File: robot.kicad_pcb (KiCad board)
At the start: 2 copper layers, 55.2 x 89.3 mm, 77 parts, among them J1 PCA9865 2, J10 BATT out, J11 Vin, J12 I2C, J2 I2S, J3 Programming, J4 IMU, J5 Switches, J6 Expansion, J7 VCC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

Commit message: Board ready to go.
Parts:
- removed J10: BATT out, Connector_PinHeader_2.54mm:Connector_Battery_SolderPads
- removed R10, R11, R12, R13, R14, R15, R16, R17, R18, R19, R20, R21, R22, R23, R24, R9: 220, Resistor_SMD:R_1206_3216Metric_Pad1.30x1.75mm_HandSolder
- removed the REF** at (143.5, 180.3)
- removed the REF** at (99.8, 139.4)
- removed the REF** at (143.5, 111.8)
- removed the REF** at (100.1, 111.8)
- added REF**: MountingHole_2.2mm_M2, MountingHole:MountingHole_2.2mm_M2, F.Cu at (146.9, 126.1)
- added REF**: MountingHole_2.2mm_M2, MountingHole:MountingHole_2.2mm_M2, F.Cu at (98.9, 95.4)
- added REF**: MountingHole_2.2mm_M2, MountingHole:MountingHole_2.2mm_M2, F.Cu at (145.8, 168.0)
- added REF**: MountingHole_2.2mm_M2, MountingHole:MountingHole_2.2mm_M2, F.Cu at (99.6, 181.7)
- added RN1: 220, Resistor_SMD:R_Array_Concave_4x0603, F.Cu at (115.1, 156.5)
- added RN2: 220, Resistor_SMD:R_Array_Concave_4x0603, F.Cu at (125.7, 156.5)
- added RN3: 220, Resistor_SMD:R_Array_Concave_4x0603, F.Cu at (110.2, 143.5)
- added RN4: 220, Resistor_SMD:R_Array_Concave_4x0603, F.Cu at (131.1, 144.5)
- moved J6 89.7 mm to (98.7, 127.7), turned to 180 degrees
- moved C12 47.1 mm to (143.8, 148.2)
- moved SW4 43.9 mm to (101.5, 133.7), turned to 180 degrees
- moved J7 42.4 mm to (139.6, 187.1), turned to -90 degrees
- moved J12 40.6 mm to (150.1, 113.0)
- moved C11 40.1 mm to (149.2, 154.2), turned to -90 degrees
- moved C10 32.6 mm to (139.7, 170.6), turned to 180 degrees
- moved C9 29.7 mm to (149.6, 161.4), turned to 90 degrees
- moved J11 29.0 mm to (120.6, 187.1), turned to -90 degrees
- moved U6 27.4 mm to (144.5, 162.4), turned to 90 degrees
- moved J5 24.0 mm to (145.1, 95.0)
- moved R28 22.5 mm to (105.3, 129.0), turned to 90 degrees
- moved D3 21.9 mm to (102.4, 125.0), turned to -90 degrees
- moved D1 17.2 mm to (113.5, 129.8)
- moved R7 15.1 mm to (111.5, 134.6), turned to 90 degrees
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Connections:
- J5 pad 1: VCC -> GND
- J5 pad 10: GND -> /SWITCH_1
- J5 pad 11: /SWITCH_4 -> GND
- J5 pad 12: GND -> /SWITCH_0
- J5 pad 13: /SWITCH_5 -> GND
- J5 pad 14: unconnected-(J5-Pad14) -> VCC
- J5 pad 2: GND -> /SWITCH_5
- J5 pad 3: /SWITCH_0 -> GND
- J5 pad 4: GND -> /SWITCH_4
- J5 pad 5: /SWITCH_1 -> GND
- J5 pad 6: GND -> /SWITCH_3
- J5 pad 7: /SWITCH_2 -> GND
- J5 pad 8: GND -> /SWITCH_2
- J5 pad 9: /SWITCH_3 -> GND
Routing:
- net GND: track 362.1 -> 463.7 mm, vias 12 -> 13
- net +BATT: track 33.1 -> 75.2 mm, vias 2 -> 0
- net Net-(C8-Pad2): track 16.9 -> 57.5 mm
- net Net-(C10-Pad2): track 0.00 -> 31.3 mm
- net IO_0: track 23.5 -> 49.1 mm
- net /ESP32_TX: track 2.52 -> 27.1 mm, vias 0 -> 1
- net /ESP32_RX: track 5.17 -> 29.1 mm, vias 1 -> 0
- net +5V: track 65.9 -> 89.3 mm
- net /SWITCH_5: track 20.9 -> 44.2 mm, vias 1 -> 2
- net IO_39: track 0.00 -> 23.1 mm, vias 0 -> 2
- net Net-(JP4-Pad7): track 26.3 -> 4.31 mm
- net VCC: track 222.7 -> 244.2 mm, vias 2 -> 5
- net Net-(JP1-Pad1): track 27.7 -> 6.45 mm, vias 1 -> 0
- net /PWM3: track 40.7 -> 19.5 mm
- net IO_36: track 0.00 -> 20.4 mm, vias 0 -> 2
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- removed copper zone on B.Cu, net GND
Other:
- board size 55.2 x 89.3 mm -> 56.3 x 97.2 mm
- board text added: "ROBOT (c)2022 J.Hudson"
- board text removed: "J1"

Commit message: Clean chematic
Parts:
- removed REF** (x4): MountingHole_2.2mm_M2, MountingHole:MountingHole_2.2mm_M2
- added C13: 104, Capacitor_SMD:C_1206_3216Metric_Pad1.33x1.80mm_HandSolder, F.Cu at (116.3, 165.0)
- added C14: 106, Capacitor_SMD:C_1210_3225Metric_Pad1.33x2.70mm_HandSolder, F.Cu at (121.0, 168.5)
- added J10: Servo pwr, Connector_PinHeader_2.54mm:Connector_SolderPadsx3, F.Cu at (98.2, 168.8)
- added J13: VCC, Connector_PinHeader_2.54mm:PinHeader_1x02_P2.54mm_Vertical, F.Cu at (99.8, 94.9)
- added JP6: HEADER-3X04, Adafruit:3X04, F.Cu at (140.7, 182.6)
- added JP7: HEADER-3X04, Adafruit:3X04, F.Cu at (106.8, 173.2)
- added JP8: HEADER-3X04, Adafruit:3X04, F.Cu at (140.8, 173.2)
- added JP9: HEADER-3X04, Adafruit:3X04, F.Cu at (106.6, 182.2)
- added R9: 10K, Resistor_SMD:R_1206_3216Metric_Pad1.30x1.75mm_HandSolder, F.Cu at (115.7, 182.0)
- added RN5: 220, Resistor_SMD:R_Array_Concave_4x0603, F.Cu at (132.3, 178.7)
- added RN6: 220, Resistor_SMD:R_Array_Concave_4x0603, F.Cu at (114.6, 169.3)
- added RN7: 220, Resistor_SMD:R_Array_Concave_4x0603, F.Cu at (133.7, 169.2)
- added RN8: 220, Resistor_SMD:R_Array_Concave_4x0603, F.Cu at (115.7, 177.8)
- added U7: PCA9685PW, Package_SO:TSSOP-28_4.4x9.7mm_P0.65mm, F.Cu at (123.7, 177.8)
- moved C12 50.3 mm to (147.2, 198.4), turned to 180 degrees
- moved U6 43.9 mm to (141.4, 206.2), turned to 0 degrees
- moved C11 35.7 mm to (145.4, 189.6), turned to 180 degrees
- moved C9 33.8 mm to (141.4, 194.2)
- moved J1 32.1 mm to (149.4, 153.8), turned to 0 degrees
- moved U3 22.9 mm to (128.7, 206.2)
- moved C4 20.9 mm to (122.2, 193.6)
- moved C5 20.9 mm to (116.1, 196.2)
- moved C8 20.9 mm to (110.6, 190.6)
- moved F1 20.9 mm to (105.2, 200.4)
- moved J11 20.9 mm to (120.6, 208.0)
- moved J9 20.9 mm to (98.0, 197.2)
- moved R26 20.9 mm to (116.1, 192.9)
- moved SW5 20.9 mm to (104.4, 207.9)
- moved U4 20.9 mm to (118.6, 188.6)
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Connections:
- RN1 pad 1: /PWM0 -> /servos/PWM3
- RN1 pad 2: /PWM1 -> /servos/PWM2
- RN1 pad 3: /PWM2 -> /servos/PWM1
- RN1 pad 4: /PWM3 -> /servos/PWM0
- RN2 pad 1: /PWM8 -> /servos/PWM11
- RN2 pad 2: /PWM9 -> /servos/PWM10
- RN2 pad 3: /PWM10 -> /servos/PWM9
- RN2 pad 4: /PWM11 -> /servos/PWM8
- RN3 pad 5: /PWM4 -> /servos/PWM7
- RN3 pad 6: /PWM5 -> /servos/PWM6
- RN3 pad 7: /PWM6 -> /servos/PWM5
- RN3 pad 8: /PWM7 -> /servos/PWM4
- RN4 pad 5: /PWM12 -> /servos/PWM15
- RN4 pad 6: /PWM13 -> /servos/PWM14
- RN4 pad 7: /PWM14 -> /servos/PWM13
- RN4 pad 8: /PWM15 -> /servos/PWM12
- U2 pad 10: /PWM4 -> /servos/PWM4
- U2 pad 11: /PWM5 -> /servos/PWM5
- U2 pad 12: /PWM6 -> /servos/PWM6
- U2 pad 13: /PWM7 -> /servos/PWM7
- U2 pad 15: /PWM8 -> /servos/PWM8
- U2 pad 16: /PWM9 -> /servos/PWM9
- U2 pad 17: /PWM10 -> /servos/PWM10
- U2 pad 18: /PWM11 -> /servos/PWM11
- U2 pad 19: /PWM12 -> /servos/PWM12
- U2 pad 20: /PWM13 -> /servos/PWM13
- U2 pad 21: /PWM14 -> /servos/PWM14
- U2 pad 22: /PWM15 -> /servos/PWM15
- U2 pad 6: /PWM0 -> /servos/PWM0
- U2 pad 7: /PWM1 -> /servos/PWM1
- U2 pad 8: /PWM2 -> /servos/PWM2
- U2 pad 9: /PWM3 -> /servos/PWM3
- U4 pad 4: +5V -> +5VL
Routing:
- net GND: track 463.7 -> 595.8 mm, vias 13 -> 16
- net +5VL: track 0.00 -> 69.3 mm
- net VCC: track 244.2 -> 308.5 mm, vias 5 -> 6
- net +5VA: track 0.00 -> 48.9 mm
- net +5VD: track 65.9 -> 100.1 mm, vias 1 -> 2
- net WIRE_1_SCL: track 97.7 -> 127.9 mm
- net WIRE_1_SDA: track 85.6 -> 114.8 mm, vias 4 -> 5
- net ONEWIRE_BUS: track 62.2 -> 90.7 mm, vias 3 -> 5
- net /servos/PWM3: track 0.00 -> 24.7 mm, vias 0 -> 2
- net /PWM0: track 24.4 -> 0.00 mm, vias 2 -> 0
- net /PWM1: track 23.2 -> 0.00 mm, vias 2 -> 0
- net /servos/PWM0: track 0.00 -> 22.3 mm, vias 0 -> 2
- net /PWM2: track 21.6 -> 0.00 mm, vias 2 -> 0
- net /servos/PWM1: track 0.00 -> 20.1 mm, vias 0 -> 2
- net /PWM3: track 19.5 -> 0.00 mm, vias 2 -> 0
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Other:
- board size 56.3 x 97.2 mm -> 56.3 x 118.2 mm

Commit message: Cleaned revision 2.
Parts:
- added ?: , , F.Cu at (98.5, 189.6)
- added ?: , , F.Cu at (146.6, 125.6)
- added ?: , , F.Cu at (150.4, 208.4)
- added ?: , , F.Cu at (103.2, 98.3)
- moved R27 9.18 mm to (117.3, 130.7), turned to 90 degrees
- moved C2 1.07 mm to (114.5, 134.7)
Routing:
- net VCC: track 308.5 -> 297.5 mm
- net IO_0: track 60.1 -> 54.6 mm
- net Net-(C10-Pad2): track 20.3 -> 22.7 mm
- net ONEWIRE_BUS: vias 5 -> 4

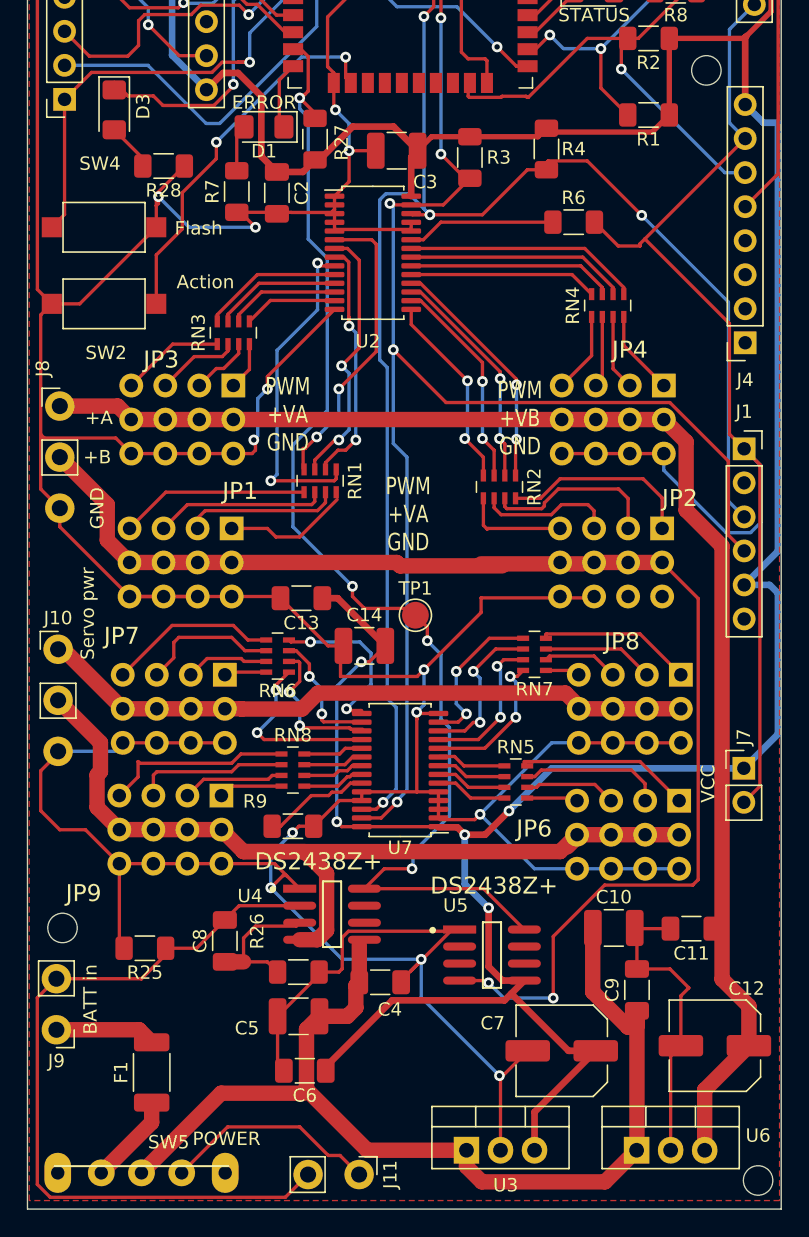
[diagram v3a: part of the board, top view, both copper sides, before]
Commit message: Very minor tweaks for board version 3.
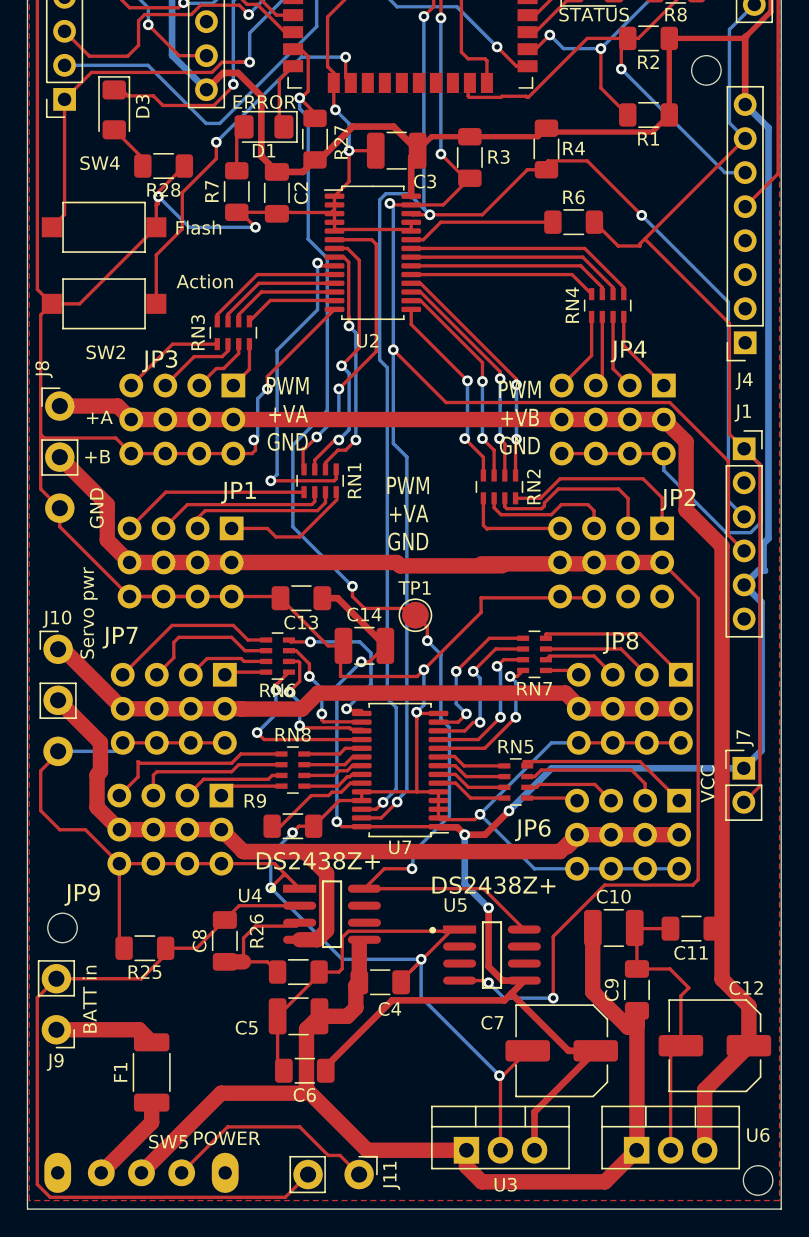
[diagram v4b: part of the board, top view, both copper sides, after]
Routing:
- net VCC: track 297.5 -> 294.6 mm

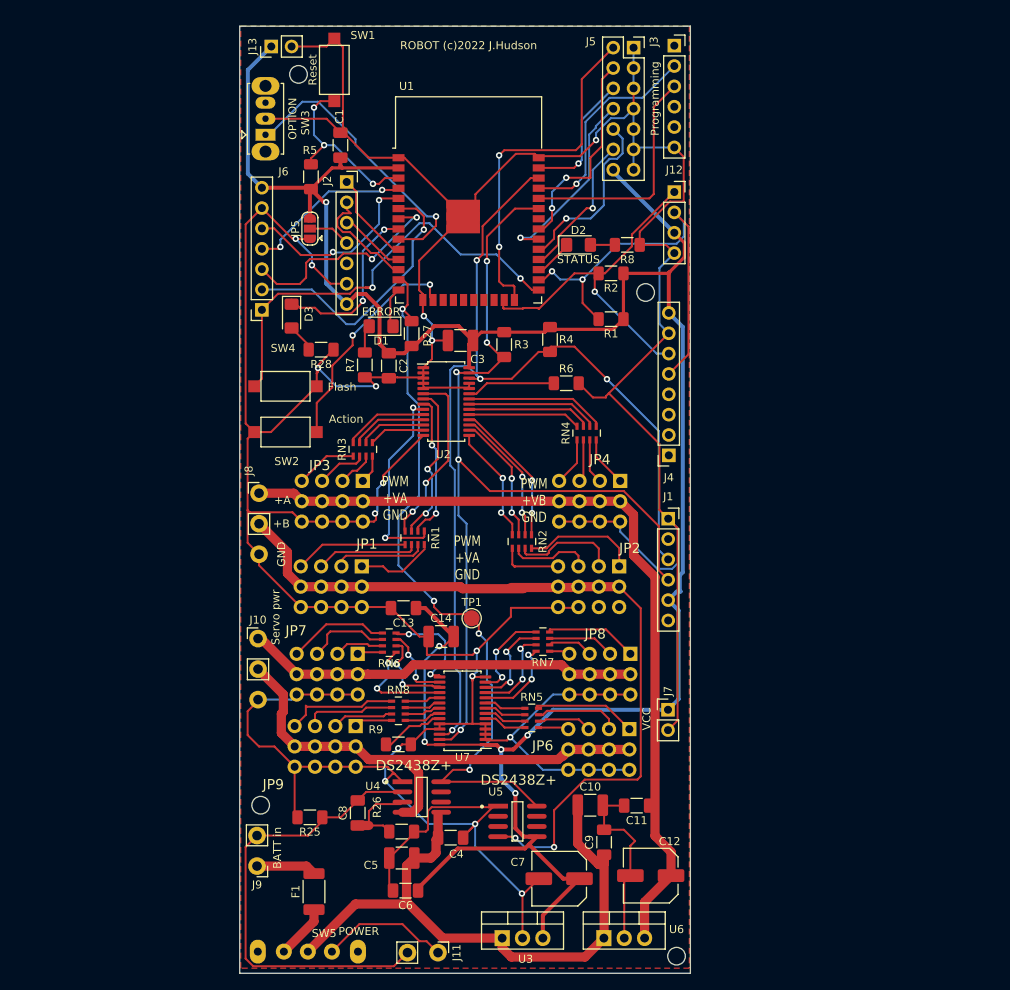
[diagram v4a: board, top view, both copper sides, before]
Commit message: Upgrade to version 7, started adding new WROOM-S3
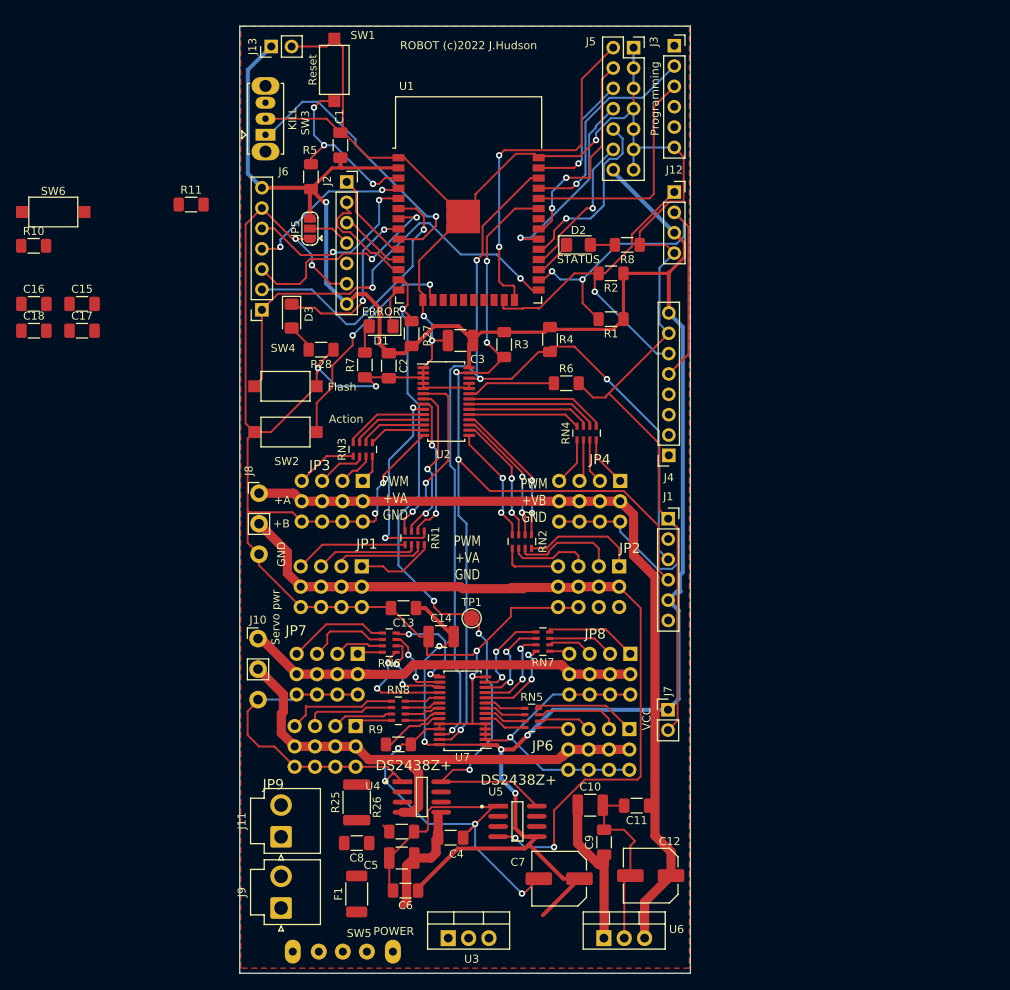
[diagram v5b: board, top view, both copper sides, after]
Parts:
- removed ? (x4): , 
- added C15: 104, Capacitor_SMD:C_1206_3216Metric_Pad1.33x1.80mm_HandSolder, F.Cu at (76.2, 127.0)
- added C16: 104, Capacitor_SMD:C_1206_3216Metric_Pad1.33x1.80mm_HandSolder, F.Cu at (70.2, 127.0)
- added C17: 104, Capacitor_SMD:C_1206_3216Metric_Pad1.33x1.80mm_HandSolder, F.Cu at (76.2, 130.3)
- added C18: 104, Capacitor_SMD:C_1206_3216Metric_Pad1.33x1.80mm_HandSolder, F.Cu at (70.2, 130.3)
- added R10: 10K, Resistor_SMD:R_1206_3216Metric_Pad1.30x1.75mm_HandSolder, F.Cu at (70.2, 119.8)
- added R11: 100K, Resistor_SMD:R_1206_3216Metric_Pad1.30x1.75mm_HandSolder, F.Cu at (89.8, 114.6)
- added SW6: OPTION, Button_Switch_SMD:SW_SPST_CK_RS282G05A3, F.Cu at (72.6, 115.5)
- J11, J9: footprint Connector_PinHeader_2.54mm:Connector_Battery_SolderPads -> Connector_JST:JST_VH_B2P-VH-B_1x02_P3.96mm_Vertical
- R25: footprint Resistor_SMD:R_1206_3216Metric_Pad1.30x1.75mm_HandSolder -> Resistor_SMD:R_1812_4532Metric_Pad1.30x3.40mm_HandSolder
- SW3: value OPTION -> KILL
- moved J11 24.3 mm to (101.0, 193.5), turned to 90 degrees
- moved U3 6.73 mm to (121.9, 206.2)
- moved R25 6.13 mm to (110.5, 189.2), turned to 90 degrees
- moved J9 6.04 mm to (101.0, 202.4), turned to 90 degrees
- moved F1 5.34 mm to (110.5, 200.7)
- moved SW5 4.37 mm to (108.8, 207.9)
- moved C8 3.76 mm to (110.5, 194.3), turned to 180 degrees
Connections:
- C10 pad 2: Net-(C10-Pad2) -> GND
- C11 pad 2: Net-(C10-Pad2) -> GND
- C12 pad 2: Net-(C10-Pad2) -> GND
- C9 pad 2: Net-(C10-Pad2) -> GND
- J6 pad 2: IO_34 -> IO_35
- J6 pad 3: IO_35 -> IO_36
- J6 pad 4: IO_36 -> IO_39
- J6 pad 5: IO_39 -> GND
- J6 pad 6: GND -> VCC
- J6 pad 7: VCC -> (no net)
- U6 pad 2: Net-(C10-Pad2) -> GND
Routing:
- net Net-(C8-Pad2): track 57.5 -> 0.00 mm
- net +BATT: track 79.0 -> 35.3 mm
- net Net-(C10-Pad2): track 22.7 -> 0.00 mm
- net Net-(J11-Pad1): track 16.1 -> 0.00 mm
- net GND: track 595.8 -> 607.2 mm
- net Net-(C8-Pad1): track 10.7 -> 1.44 mm
- net Net-(F1-Pad2): track 7.50 -> 0.00 mm
- net Net-(F1-Pad1): track 6.80 -> 0.00 mm
- net VCC: track 294.6 -> 291.7 mm

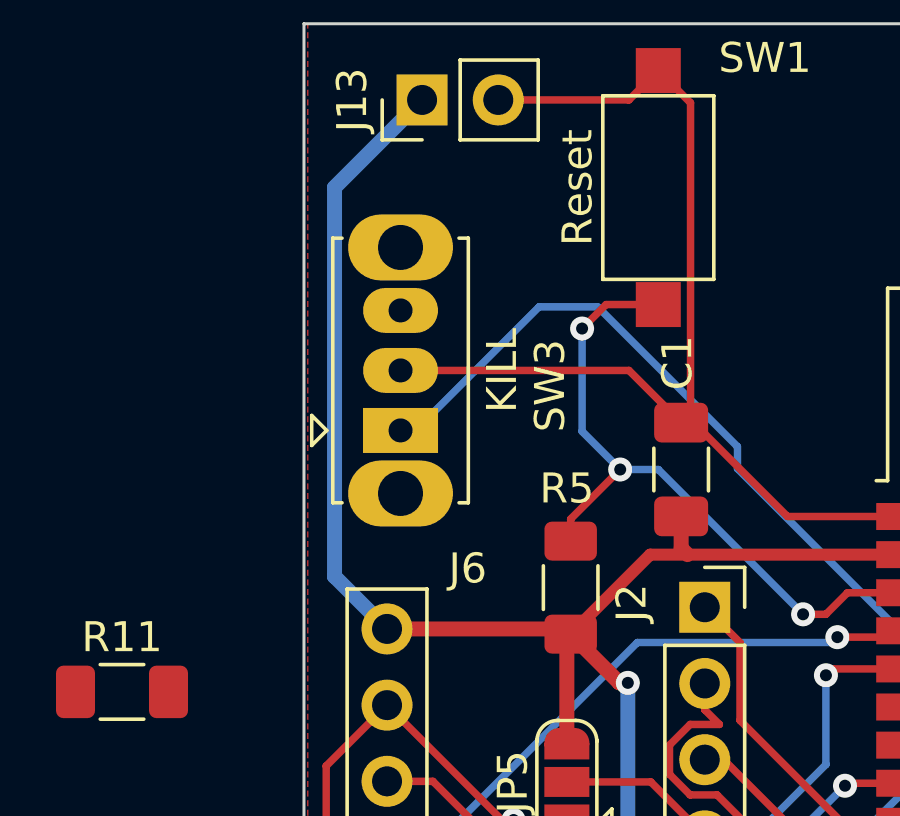
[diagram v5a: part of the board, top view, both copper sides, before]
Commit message: started wiring up s3
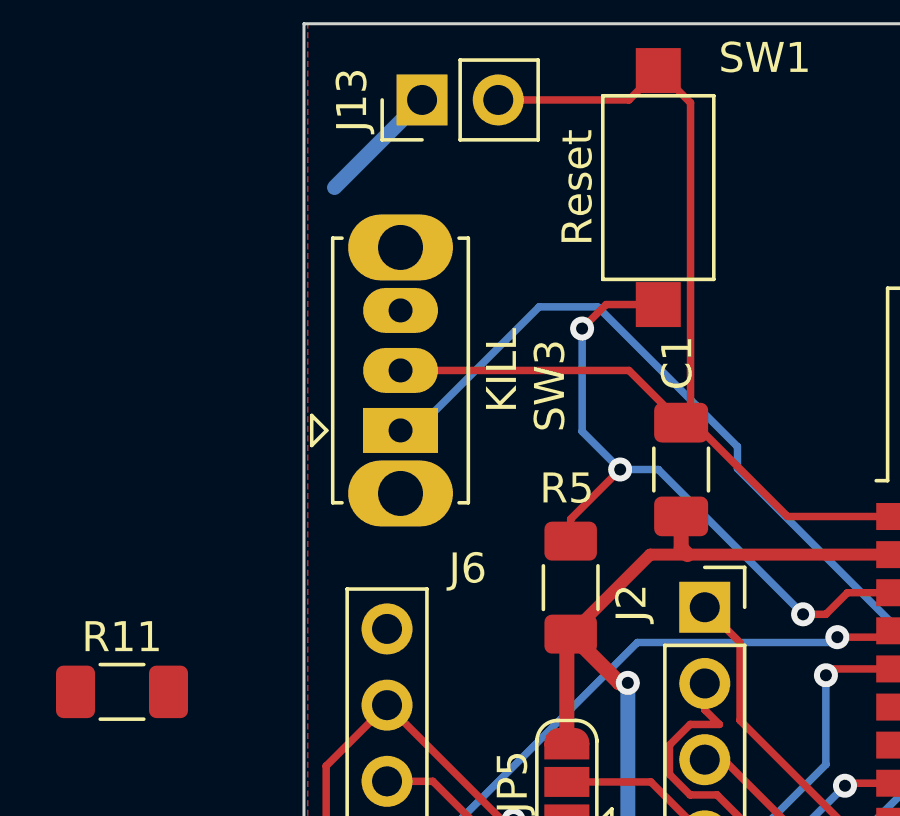
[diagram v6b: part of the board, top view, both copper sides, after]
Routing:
- net VCC: track 291.7 -> 270.3 mm
